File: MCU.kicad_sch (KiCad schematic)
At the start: 12 parts, among them SW301 RESET, U202 NUCLEO64-H503RB

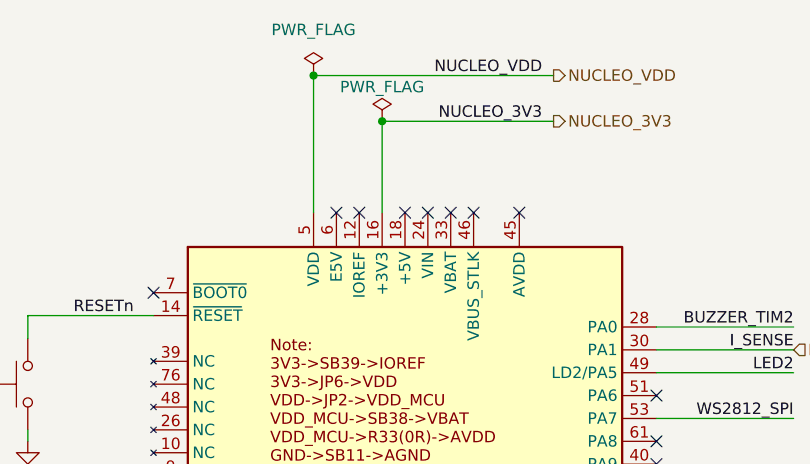
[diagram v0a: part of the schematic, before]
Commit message: Continued routing + resized the board
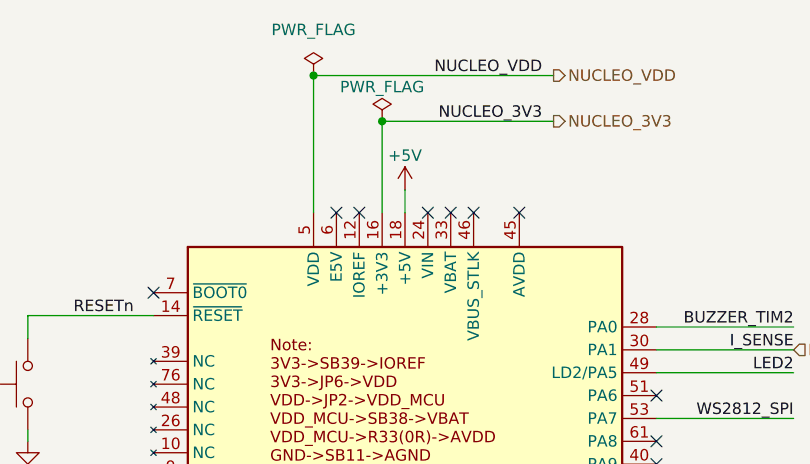
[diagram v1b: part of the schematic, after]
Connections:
- net +5V: now reaches U202.18 (+5V)
- no-connect marks 36 -> 35
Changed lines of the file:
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@@
-	)
-	(no_connect
-		(at 92.71 44.45)
 	)
 	(no_connect
@@
 		(pts
 			(xy 207.01 60.96) (xy 220.98 60.96)
+		)
+		(stroke
+			(width 0)
+			(type default)
+		)
+	)
+	(wire
+		(pts
+			(xy 92.71 41.91) (xy 92.71 44.45)
 		)
 		(stroke
@@
 					(unit 1)
 				)
+			)
+		)
+	)
+	(symbol
+		(lib_id "power:+5V")
+		(at 92.71 41.91 0)
+		(unit 1)
+		(exclude_from_sim no)
+		(in_bom yes)
+		(on_board yes)
+		(dnp no)
+		(property "Reference" "#PWR0306"
+			(at 92.71 45.72 0)
+			(effects
+				(font
+					(size 1.27 1.27)
+				)
+				(hide yes)
+			)
+		)
+		(property "Value" "+5V"
+			(at 92.71 38.1 0)
+			(effects
+				(font
+					(size 1.27 1.27)
+				)
+			)
+		)
+		(property "Footprint" ""
+			(at 92.71 41.91 0)
+			(effects
+				(font
+					(size 1.27 1.27)
+				)
+				(hide yes)
+			)
+		)
+		(property "Datasheet" ""
+			(at 92.71 41.91 0)
+			(effects
+				(font
+					(size 1.27 1.27)
+				)
+				(hide yes)
+			)
+		)
+		(property "Description" "Power symbol creates a global label with name \"+5V\""
+			(at 92.71 41.91 0)
+			(effects
+				(font
+					(size 1.27 1.27)
+				)
+				(hide yes)
+			)
+		)
+		(pin "1"
+		)
+		(instances
+			(project "Educational-Board_MainBoard"
+				(path "/835b4df9-7d62-45f4-81d2-5a64fbc86f3c/a718e7a0-c449-4532-ac19-5f778084acdd"
+					(reference "#PWR0306")
+					(unit 1)
+				)

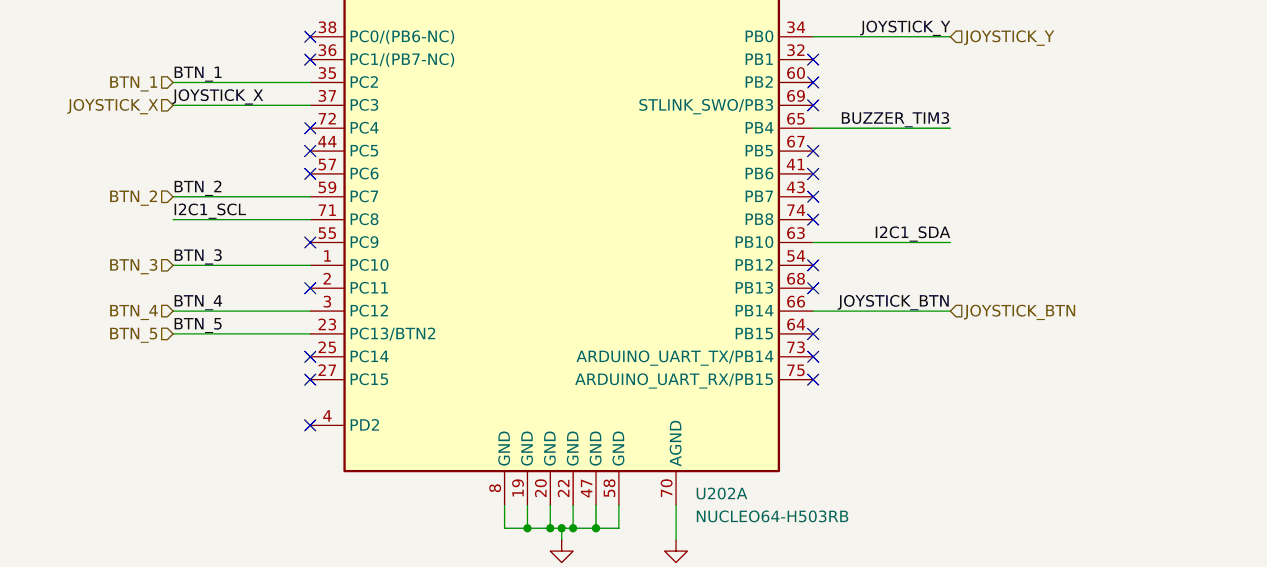
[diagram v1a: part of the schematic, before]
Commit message: Routed most LEFT part of the board + modified button footprint + fixed some lables
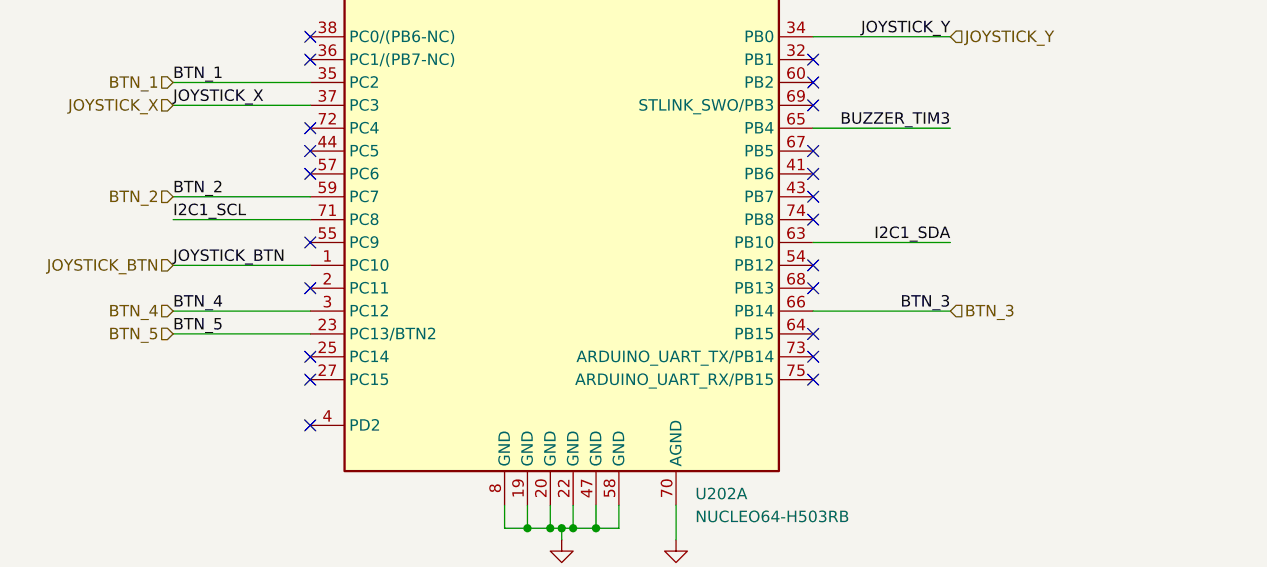
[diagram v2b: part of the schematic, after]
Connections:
- net BTN_3: now also U202.66 (PB14); no longer U202.1 (PC10)
- net JOYSTICK_BTN: now also U202.1 (PC10); no longer U202.66 (PB14)
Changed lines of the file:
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@@
+	(wire
+		(pts
+			(xy 135.89 124.46) (xy 120.65 124.46)
+		)
+		(stroke
+			(width 0)
+			(type default)
+		)
+	)
 	(wire
 		(pts
@@
 	(wire
 		(pts
-			(xy 120.65 124.46) (xy 135.89 124.46)
-		)
-		(stroke
-			(width 0)
-			(type default)
-		)
-	)
-	(wire
-		(pts
 			(xy 226.06 53.34) (xy 232.41 53.34)
 		)
@@
 	(wire
 		(pts
-			(xy 49.53 119.38) (xy 64.77 119.38)
-		)
-		(stroke
-			(width 0)
-			(type default)
-		)
-	)
-	(wire
-		(pts
 			(xy 82.55 29.21) (xy 109.22 29.21)
 		)
@@
 		(pts
 			(xy 91.44 146.05) (xy 91.44 148.59)
+		)
+		(stroke
+			(width 0)
+			(type default)
+		)
+	)
+	(wire
+		(pts
+			(xy 64.77 119.38) (xy 49.53 119.38)
 		)
 		(stroke
@@
 		)
 	)
+	(label "JOYSTICK_BTN"
+		(at 49.53 119.38 0)
+		(effects
+			(font
+				(size 1.27 1.27)
+			)
+			(justify left bottom)
+		)
+	)
 	(label "JOYSTICK_X"
 		(at 49.53 101.6 0)
@@
 		)
 	)
+	(label "BTN_3"
+		(at 135.89 124.46 180)
+		(effects
+			(font
+				(size 1.27 1.27)
+			)
+			(justify right bottom)
+		)
+	)
 	(label "I_SENSE"
 		(at 135.89 59.69 180)
@@
 		)
 	)
-	(label "JOYSTICK_BTN"
-		(at 135.89 124.46 180)
-		(effects
-			(font
-				(size 1.27 1.27)
-			)
-			(justify right bottom)
-		)
-	)
 	(label "NUCLEO_VDD"
 		(at 107.95 29.21 180)
@@
 			)
 			(justify right bottom)
-		)
-	)
-	(label "BTN_3"
-		(at 49.53 119.38 0)
-		(effects
-			(font
-				(size 1.27 1.27)
-			)
-			(justify left bottom)
 		)
 	)
@@
 		)
 	)
+	(hierarchical_label "BTN_3"
+		(shape input)
+		(at 135.89 124.46 0)
+		(effects
+			(font
+				(size 1.27 1.27)
+			)
+			(justify left)
+		)
+	)
+	(hierarchical_label "JOYSTICK_BTN"
+		(shape input)
+		(at 49.53 119.38 180)
+		(effects
+			(font
+				(size 1.27 1.27)
+			)
+			(justify right)
+		)
+	)
 	(hierarchical_label "I2C_SDA"
 		(shape bidirectional)
@@
 		)
 	)
-	(hierarchical_label "BTN_3"
-		(shape input)
-		(at 49.53 119.38 180)
-		(effects
-			(font
-				(size 1.27 1.27)
-			)
-			(justify right)
-		)
-	)
 	(hierarchical_label "I2C_SCL"
 		(shape bidirectional)
@@
 		(effects
 			(font
-				(size 1.27 1.27)
-			)
-			(justify left)
-		)
-	)
-	(hierarchical_label "JOYSTICK_BTN"
-		(shape input)
-		(at 135.89 124.46 0)
-		(effects
-			(font

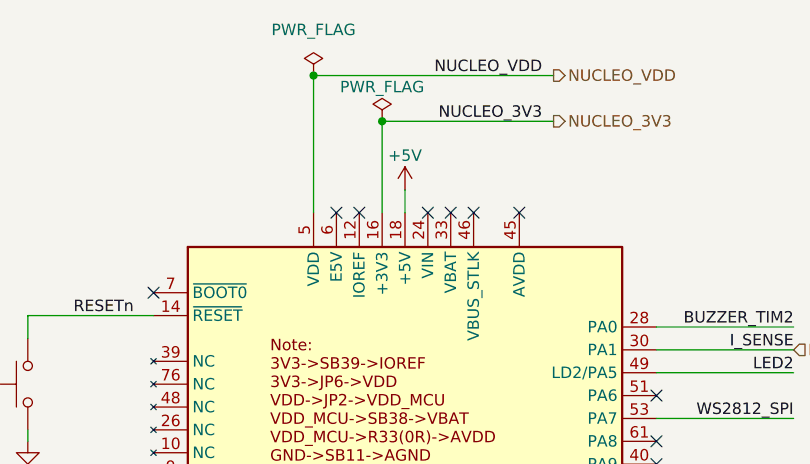
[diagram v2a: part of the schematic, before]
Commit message: Finished the routing: TODO fixing IMU
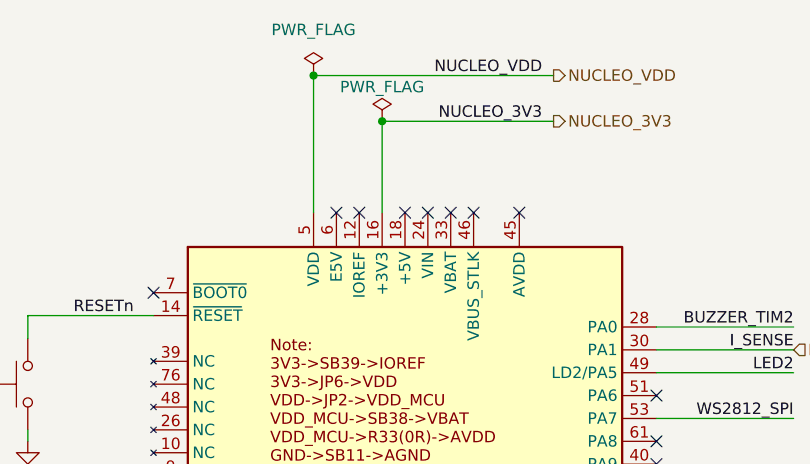
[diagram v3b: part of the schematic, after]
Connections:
- net +5V: no longer names the net of U202.18 (+5V)
- no-connect marks 35 -> 36
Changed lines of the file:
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@@
+	)
+	(no_connect
+		(at 92.71 44.45)
 	)
 	(no_connect
@@
 		(pts
 			(xy 207.01 60.96) (xy 220.98 60.96)
-		)
-		(stroke
-			(width 0)
-			(type default)
-		)
-	)
-	(wire
-		(pts
-			(xy 92.71 41.91) (xy 92.71 44.45)
 		)
 		(stroke
@@
 					(unit 1)
 				)
-			)
-		)
-	)
-	(symbol
-		(lib_id "power:+5V")
-		(at 92.71 41.91 0)
-		(unit 1)
-		(exclude_from_sim no)
-		(in_bom yes)
-		(on_board yes)
-		(dnp no)
-		(property "Reference" "#PWR0306"
-			(at 92.71 45.72 0)
-			(effects
-				(font
-					(size 1.27 1.27)
-				)
-				(hide yes)
-			)
-		)
-		(property "Value" "+5V"
-			(at 92.71 38.1 0)
-			(effects
-				(font
-					(size 1.27 1.27)
-				)
-			)
-		)
-		(property "Footprint" ""
-			(at 92.71 41.91 0)
-			(effects
-				(font
-					(size 1.27 1.27)
-				)
-				(hide yes)
-			)
-		)
-		(property "Datasheet" ""
-			(at 92.71 41.91 0)
-			(effects
-				(font
-					(size 1.27 1.27)
-				)
-				(hide yes)
-			)
-		)
-		(property "Description" "Power symbol creates a global label with name \"+5V\""
-			(at 92.71 41.91 0)
-			(effects
-				(font
-					(size 1.27 1.27)
-				)
-				(hide yes)
-			)
-		)
-		(pin "1"
-		)
-		(instances
-			(project "Educational-Board_MainBoard"
-				(path "/835b4df9-7d62-45f4-81d2-5a64fbc86f3c/a718e7a0-c449-4532-ac19-5f778084acdd"
-					(reference "#PWR0306")
-					(unit 1)
-				)

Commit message: routing and silkscreen logo
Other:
- company: Filippo Castellan, Alan Masutti -> Alan Masutti, Filippo Castellan
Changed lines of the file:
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@@
 		(date "2026-03-12")
 		(rev "1.0")
-		(company "Filippo Castellan, Alan Masutti")
+		(company "Alan Masutti, Filippo Castellan")
 	)
 	(junction

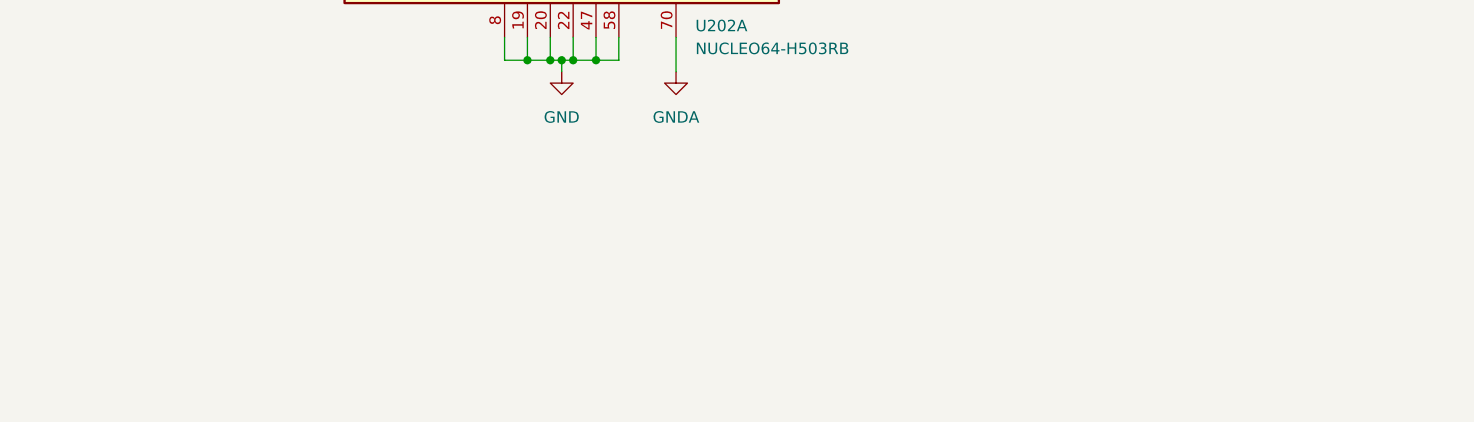
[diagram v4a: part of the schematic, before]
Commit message: Added placeholders connectors for the Nucleo - TO ADD LCSC CODES
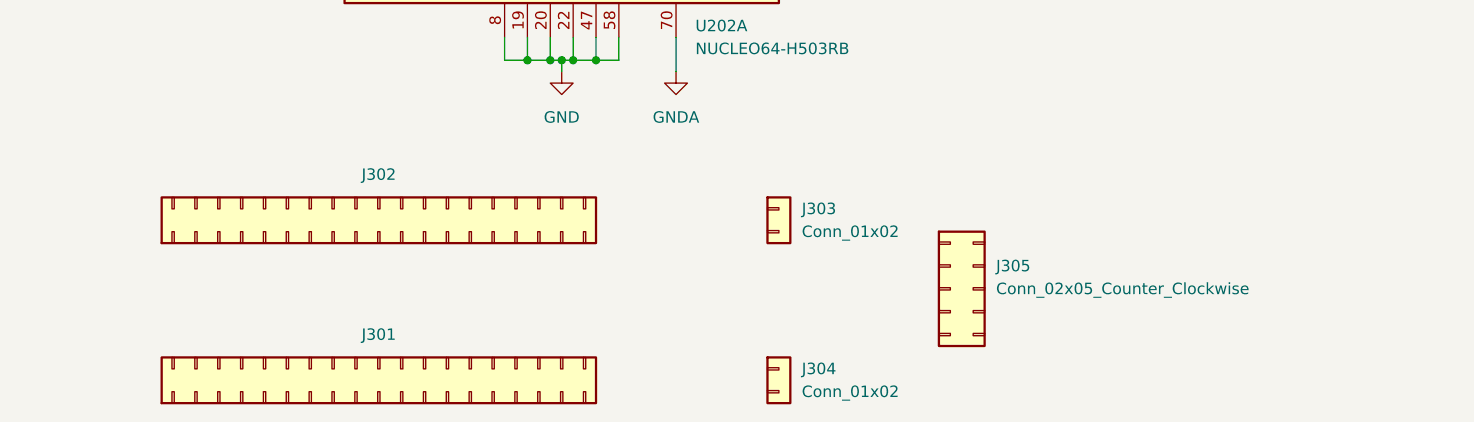
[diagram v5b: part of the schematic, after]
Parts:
- added J301, J302: Conn_02x20_Counter_Clockwise, ProjectConnectors:PLACEHOLDER_PinSocket_2x19_P2.54mm_Vertical, symbol ProjectMCUs:PLACEHOLDER_Conn_02x19_Odd_Even
- added J303, J304: Conn_01x02, ProjectConnectors:PLACEHOLDER_PinSocket_1x02_P2.54mm_Vertical, symbol ProjectMCUs:PLACEHOLDER_Conn_01x02
- added J305: Conn_02x05_Counter_Clockwise, ProjectConnectors:PLACEHOLDER_PinSocket_2x05_P2.54mm_Vertical, symbol ProjectMCUs:PLACEHOLDER_Conn_02x05_Odd_Even

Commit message: added version marking, generated all the production files, added last connector lcsc number
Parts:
- J301, J302: Checked (none) -> OK; LCSC (none) -> C2977589
- J303, J304: Checked C492401 -> OK; LCSC (none) -> C492401
- J305: Checked (none) -> OK; LCSC (none) -> C92270
- U202: now not fitted
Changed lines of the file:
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@@
 			)
 		)
-		(property "Checked" "C492401"
+		(property "Checked" "OK"
+			(at 116.84 165.1 0)
+			(effects
+				(font
+					(size 1.27 1.27)
+				)
+				(hide yes)
+			)
+		)
+		(property "LCSC" "C492401"
 			(at 116.84 165.1 0)
 			(effects
@@
 		(in_bom no)
 		(on_board yes)
-		(dnp no)
+		(dnp yes)
 		(fields_autoplaced yes)
 		(property "Reference" "U202"
@@
 			)
 		)
+		(property "Checked" "OK"
+			(at 72.39 167.64 90)
+			(effects
+				(font
+					(size 1.27 1.27)
+				)
+				(hide yes)
+			)
+		)
+		(property "LCSC" "C2977589"
+			(at 72.39 167.64 90)
+			(effects
+				(font
+					(size 1.27 1.27)
+				)
+				(hide yes)
+			)
+		)
 		(instances
 			(project "Educational-Board_MainBoard"
@@
 			)
 		)
-		(property "Checked" "C492401"
+		(property "Checked" "OK"
+			(at 116.84 182.88 0)
+			(effects
+				(font
+					(size 1.27 1.27)
+				)
+				(hide yes)
+			)
+		)
+		(property "LCSC" "C492401"
 			(at 116.84 182.88 0)
 			(effects
@@
 			)
 		)
+		(property "Checked" "OK"
+			(at 72.39 185.42 90)
+			(effects
+				(font
+					(size 1.27 1.27)
+				)
+				(hide yes)
+			)
+		)
+		(property "LCSC" "C2977589"
+			(at 72.39 185.42 90)
+			(effects
+				(font
+					(size 1.27 1.27)
+				)
+				(hide yes)
+			)
+		)
 		(instances
 			(project "Educational-Board_MainBoard"
@@
 			(at 135.89 173.99 0)
 			(effects
+				(font
+					(size 1.27 1.27)
+				)
+				(hide yes)
+			)
+		)
+		(property "Checked" "OK"
+			(at 135.89 173.99 0)
+			(effects
+				(font
+					(size 1.27 1.27)
+				)
+				(hide yes)
+			)
+		)
+		(property "LCSC" "C92270"
+			(at 135.89 173.99 0)
+			(effects

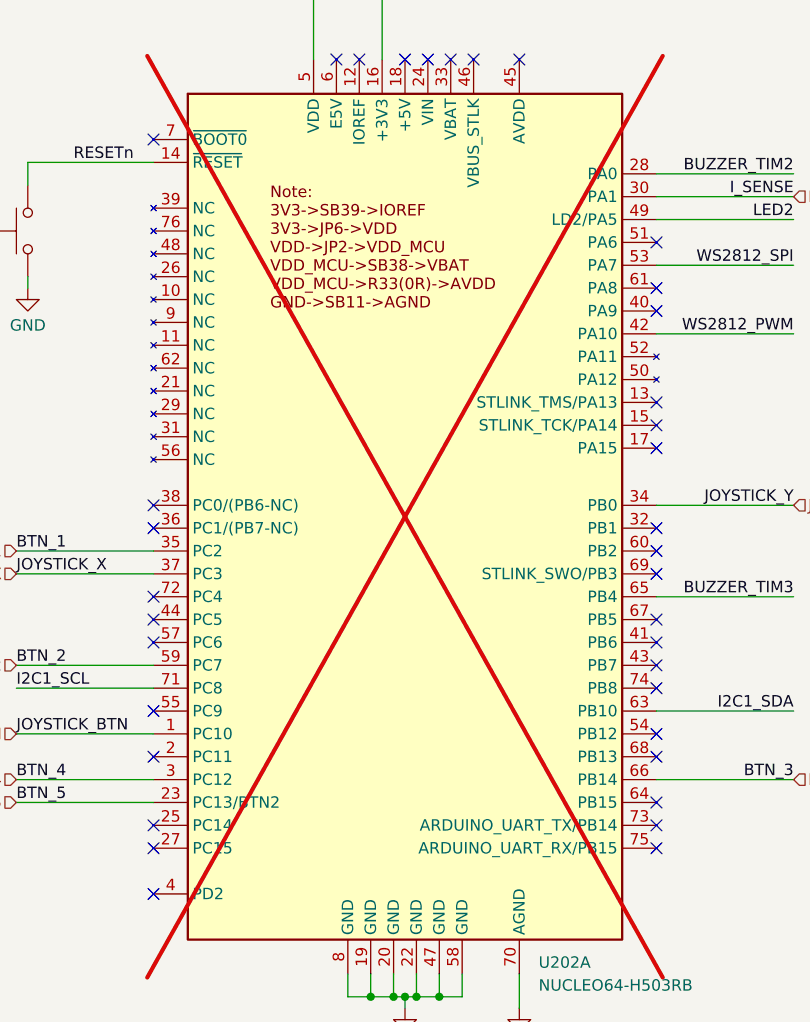
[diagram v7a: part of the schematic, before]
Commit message: Changed the Nucleo Symbol to add Arduino Names +  Rotated a I2C jumper near the LCD
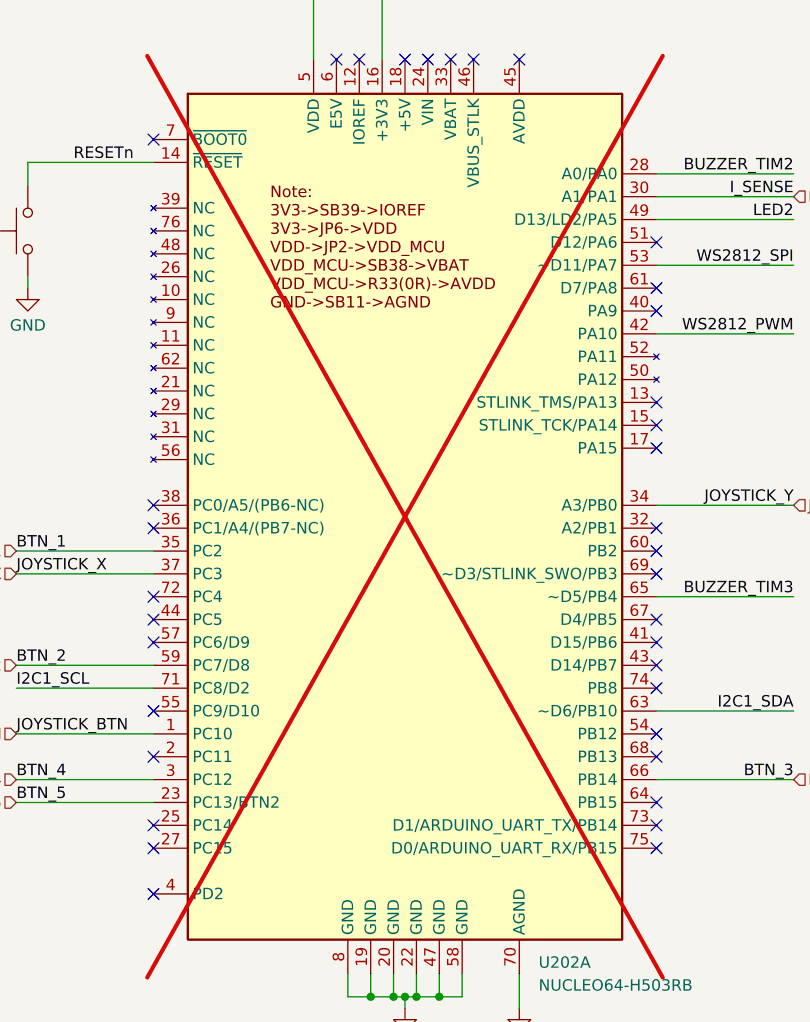
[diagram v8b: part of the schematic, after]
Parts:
- U202: footprint ProjectConnectors:Nucleo64_ST-Morpho -> ProjectConnectors:Nucleo64
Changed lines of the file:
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@@
 			)
 		)
-		(property "Footprint" "ProjectConnectors:Nucleo64_ST-Morpho"
+		(property "Footprint" "ProjectConnectors:Nucleo64"
 			(at 65.532 128.778 0)
 			(effects
